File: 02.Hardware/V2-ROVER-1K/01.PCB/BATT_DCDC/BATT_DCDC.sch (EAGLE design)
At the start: 49 parts, among them J1 DF40C-20DP-0.4V_51_, K1 FLEX8, Q1 NVTFS9D6P04M8LTAG, Q2 2N7002PW, Q5 2N7002PW, U1 MCP6071T-E/OT, U3 TPS55330RTET, U7 MCP6071T-E/OT

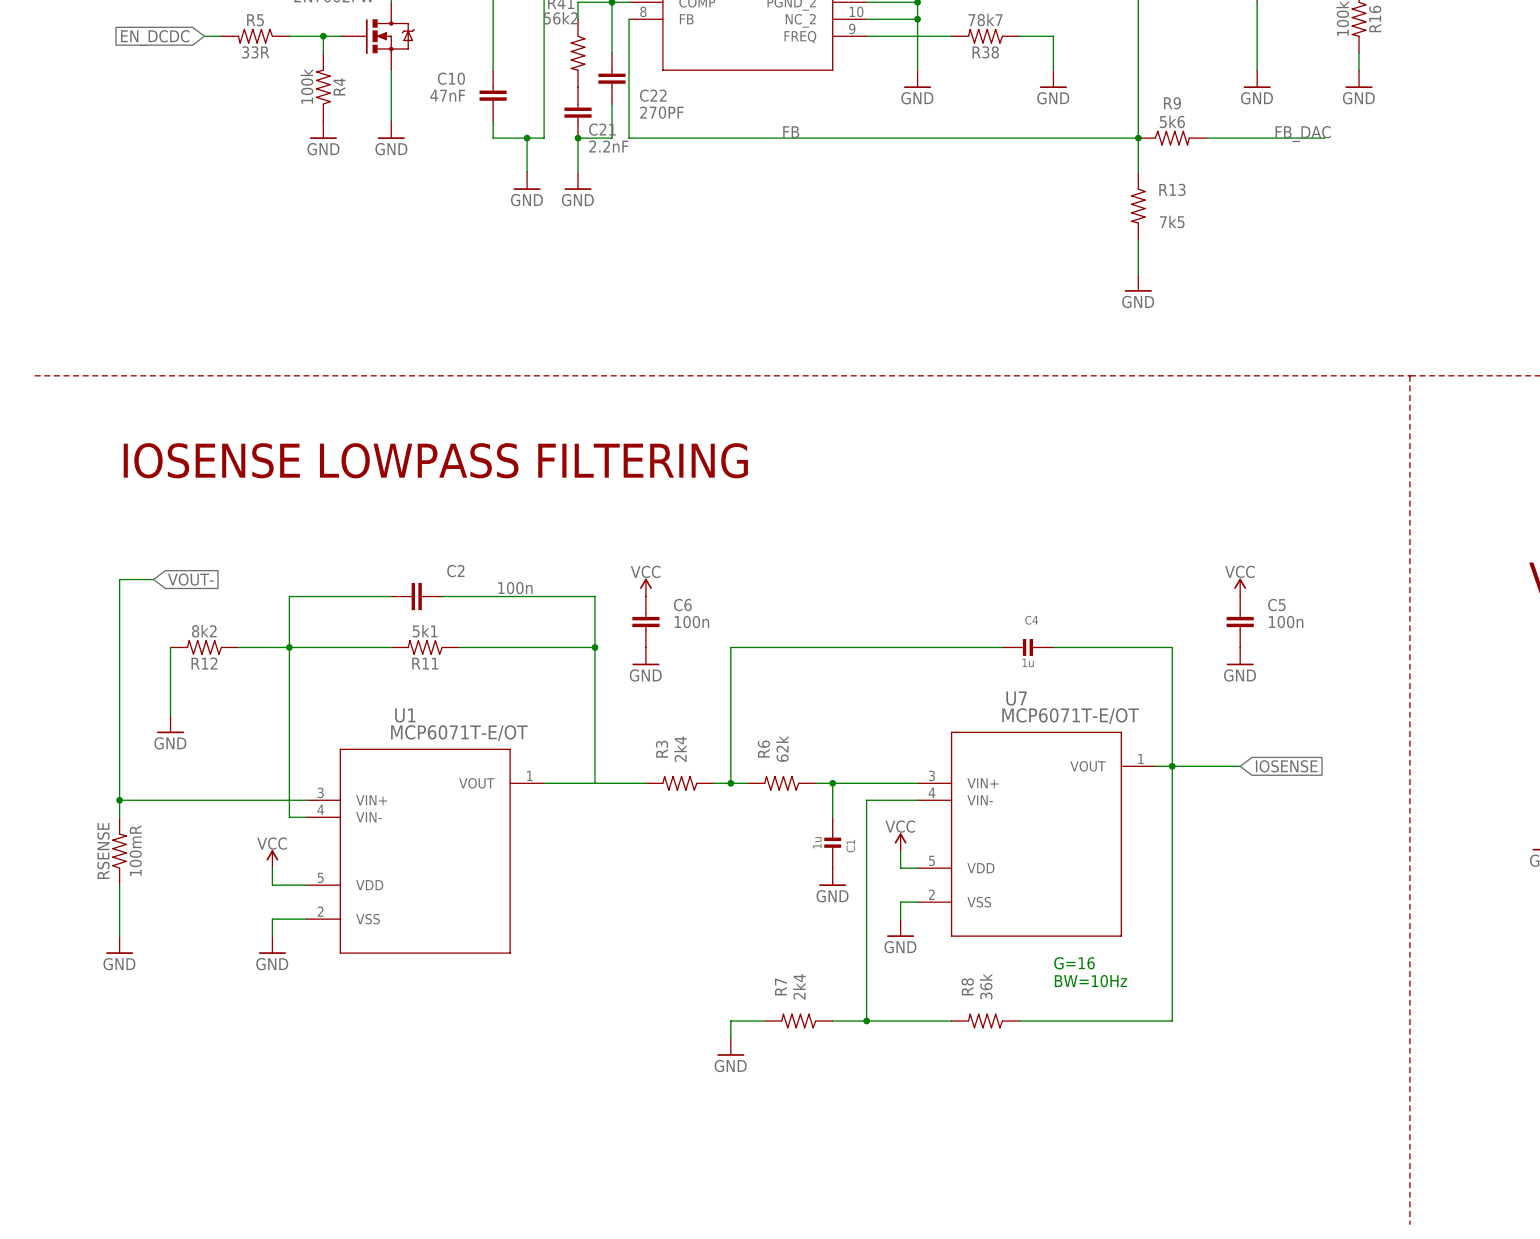
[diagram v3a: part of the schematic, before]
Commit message: Cambios menores durante revision de proto_1 de SETI
en el esquematico se incluye la frecuencia del FPB del sensado de corriente
en la BRD se aumenta el ancho de la pista de resistencia del DAC
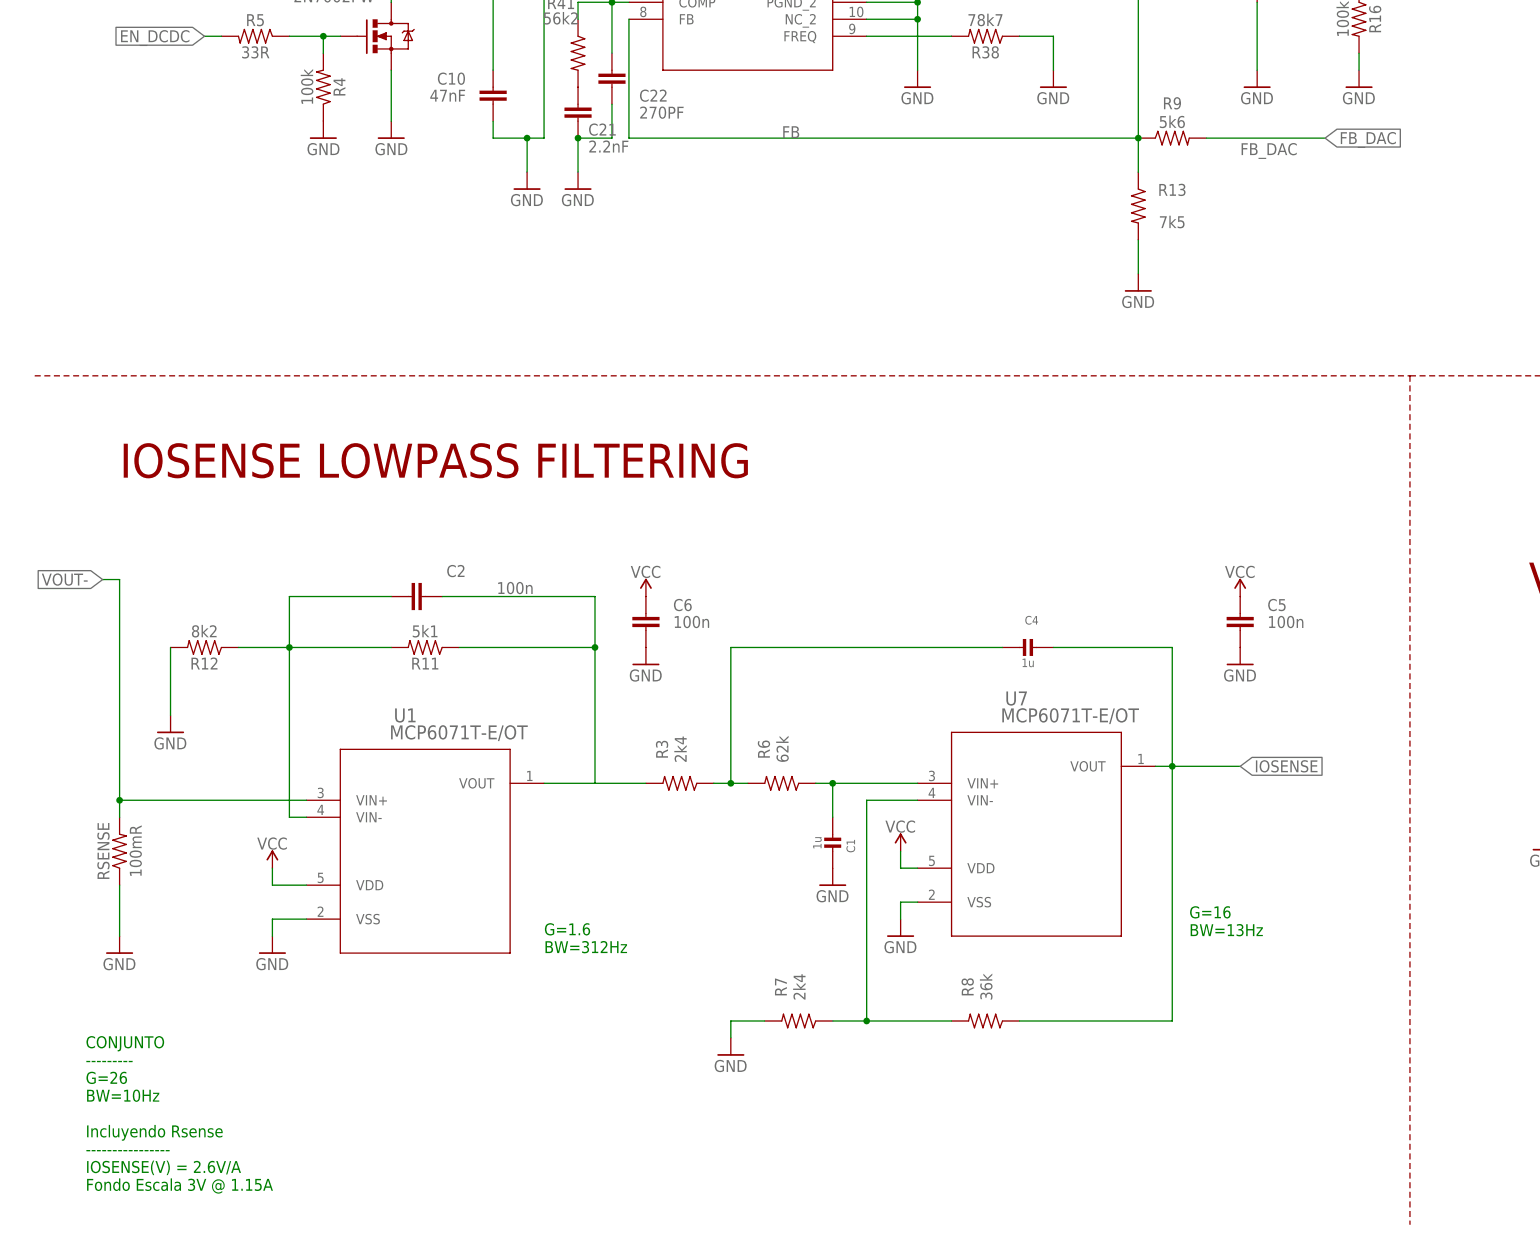
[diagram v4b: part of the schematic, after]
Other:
- note added: "CONJUNTO --------- G=26 BW=10Hz Incluyendo Rsense ---------------- IOSENSE(V) = 2.6V/A Fondo Escala 3V @ 1.15A"
- note added: "G=1.6 BW=312Hz"
- note added: "G=16 BW=13Hz"
- note removed: "G=16 BW=10Hz"
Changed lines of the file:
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@@
 <drawing>
 <settings>
-<setting alwaysvectorfont="yes"/>
+<setting alwaysvectorfont="no"/>
 <setting keepoldvectorfont="yes"/>
 <setting verticaltext="up"/>
@@
 3.0 v @ vi=16v</text>
 <text x="228.6" y="99.06" size="5.08" layer="94">VOUT SENSE</text>
-<text x="157.48" y="40.64" size="1.778" layer="91">G=16
-BW=10Hz</text>
+<text x="177.8" y="48.26" size="1.778" layer="91">G=16
+BW=13Hz</text>
 <wire x1="5.08" y1="132.08" x2="210.82" y2="132.08" width="0.1524" layer="94" style="shortdash"/>
 <wire x1="210.82" y1="132.08" x2="287.02" y2="132.08" width="0.1524" layer="94" style="shortdash"/>
@@
 <text x="35.56" y="241.3" size="5.08" layer="94">STEP UP DCDC CONVERTER
 ROVER1K - NOV'22-v1</text>
+<text x="81.28" y="45.72" size="1.778" layer="91">G=1.6
+BW=312Hz</text>
+<text x="12.7" y="10.16" size="1.778" layer="91">CONJUNTO
+---------
+G=26
+BW=10Hz
+Incluyendo Rsense
+----------------
+IOSENSE(V) = 2.6V/A
+Fondo Escala 3V @ 1.15A</text>
 </plain>
 <instances>
@@
 <pinref part="R9" gate="G$1" pin="2"/>
 <wire x1="180.34" y1="167.64" x2="198.12" y2="167.64" width="0.1524" layer="91"/>
-<label x="190.5" y="167.64" size="1.778" layer="95"/>
+<label x="185.42" y="165.1" size="1.778" layer="95"/>
+<label x="198.12" y="167.64" size="1.778" layer="95" xref="yes"/>
 </segment>
 <segment>
@@
 <wire x1="17.78" y1="66.04" x2="17.78" y2="68.58" width="0.1524" layer="91"/>
 <wire x1="17.78" y1="68.58" x2="17.78" y2="101.6" width="0.1524" layer="91"/>
-<wire x1="17.78" y1="101.6" x2="22.86" y2="101.6" width="0.1524" layer="91"/>
-<label x="22.86" y="101.6" size="1.778" layer="95" xref="yes"/>
+<wire x1="17.78" y1="101.6" x2="15.24" y2="101.6" width="0.1524" layer="91"/>
+<label x="15.24" y="101.6" size="1.778" layer="95" rot="MR0" xref="yes"/>
 <pinref part="U1" gate="A" pin="VIN+"/>
 <wire x1="45.72" y1="68.58" x2="17.78" y2="68.58" width="0.1524" layer="91"/>

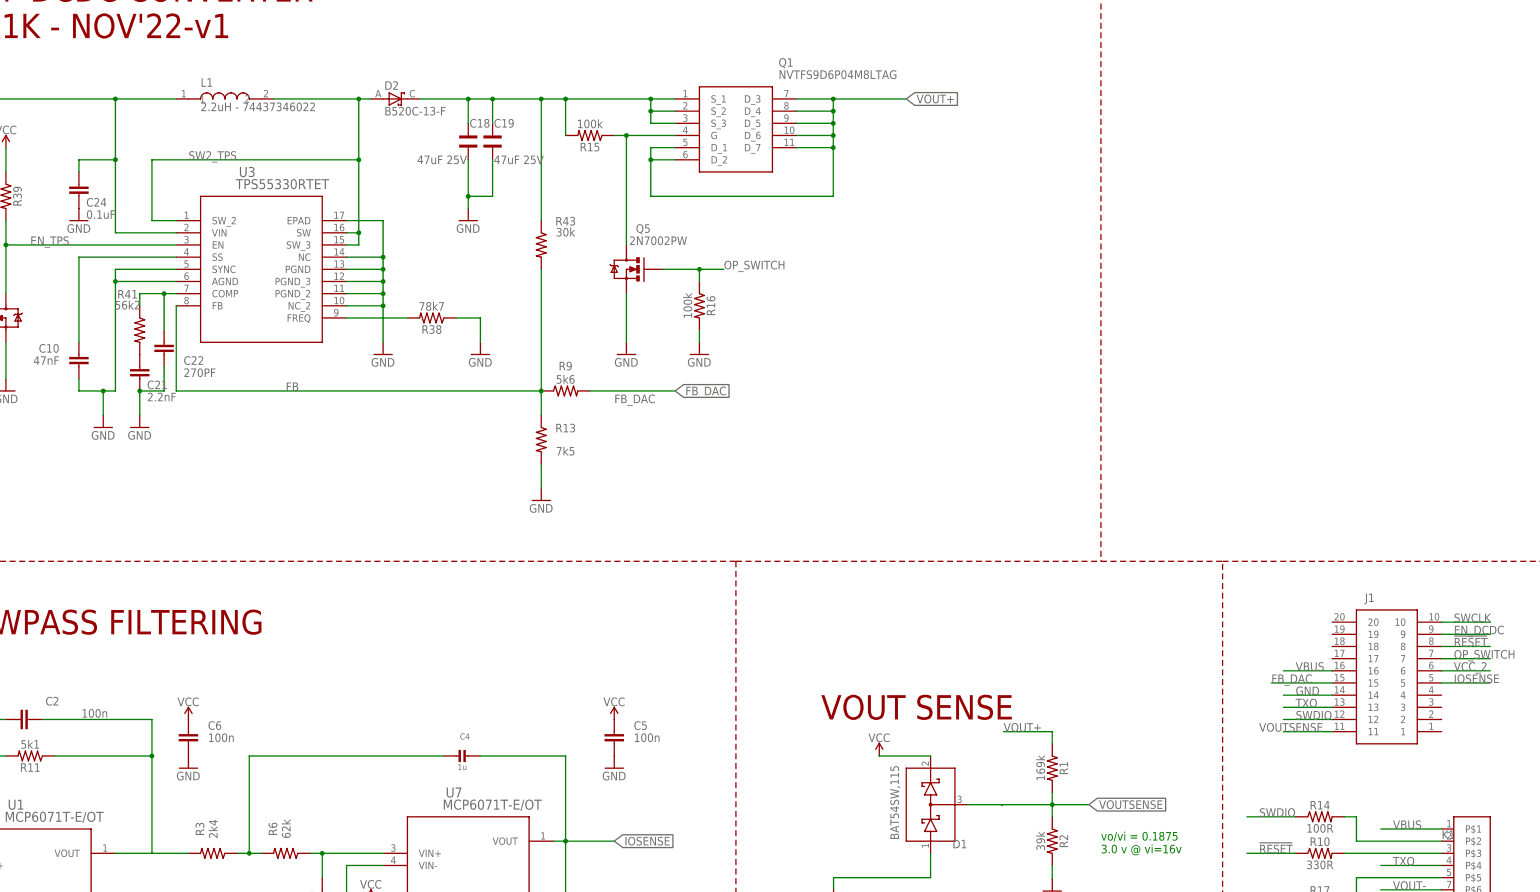
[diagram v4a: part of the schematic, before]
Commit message: Modificaciones despues de revisar 1er prototipo de SETI
Se van añadiendo modificaciones, pero no están todas las que son necesarias.
Este es el fichero que le paso a Javi para  que comience con el resto de los cambios.
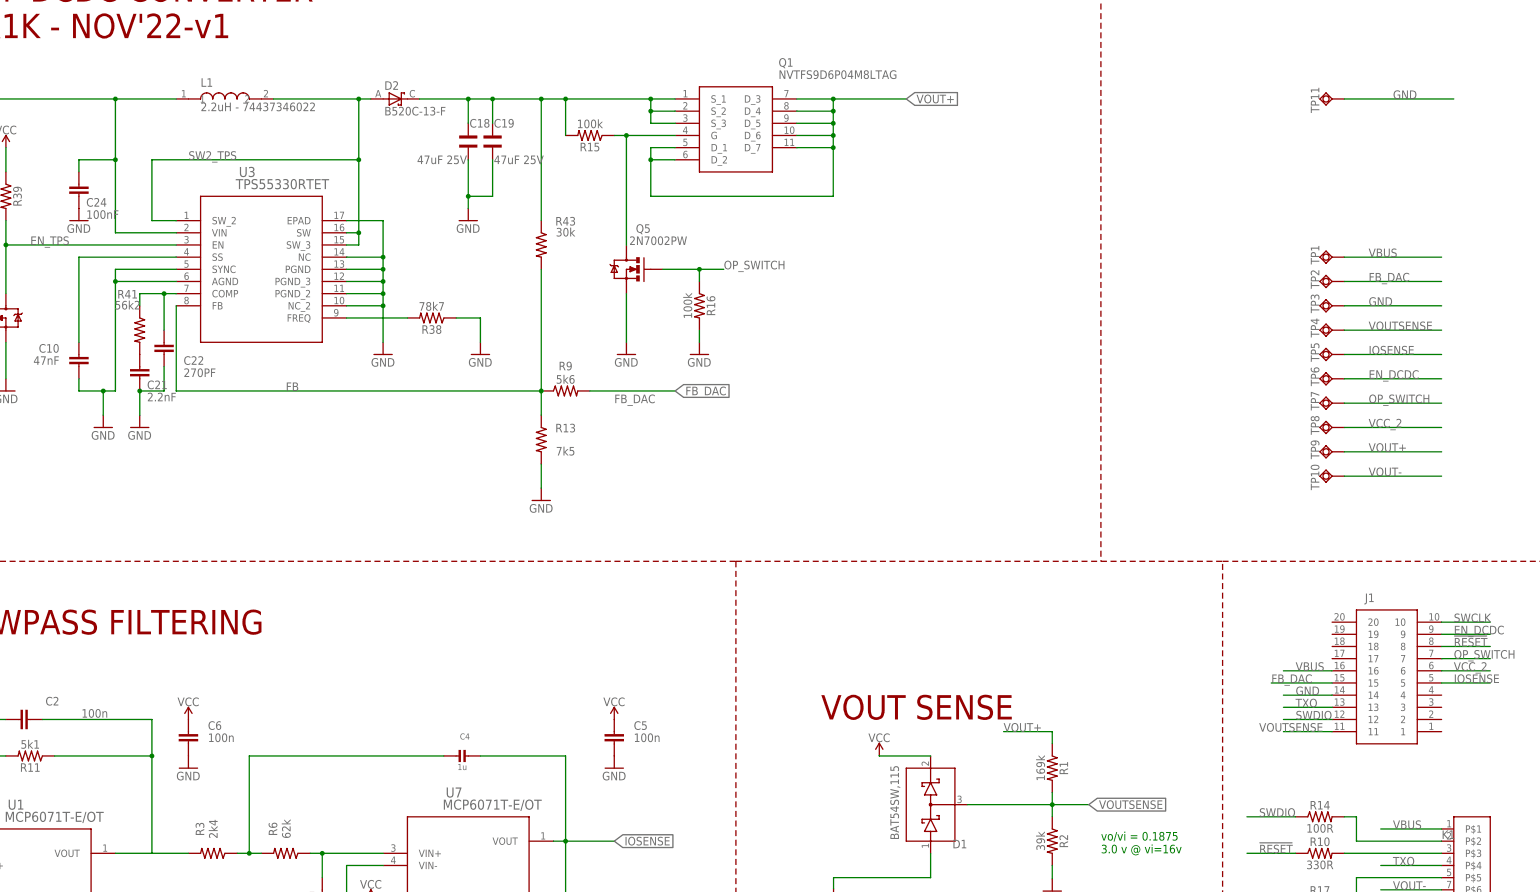
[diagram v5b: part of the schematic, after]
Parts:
- added TP1, TP10, TP11, TP2, TP3, TP4, TP5, TP6, TP7, TP8, TP9: TESTPAD_TPSQB1,27, BeagleBone_Blue_R3:TESTPAD_TPSQB1,27
- C24: value 0.1uF -> 100nF
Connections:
- net EN_DCDC: now also TP6.TP
- net FB_DAC: now also TP2.TP
- net GND: now also TP11.TP, TP3.TP
- net IOSENSE: now also TP5.TP
- net OP_SWITCH: now also TP7.TP
- net VBUS: now also TP1.TP
- net VCC_2: now also TP8.TP
- net VOUT+: now also TP9.TP
- net VOUT-: now also TP10.TP
- net VOUTSENSE: now also TP4.TP

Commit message: Cambios DCDC Javi Version Final. Pendiente de revision
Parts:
- removed TP1, TP10, TP11, TP2, TP3, TP4, TP5, TP6, TP7, TP8, TP9: TESTPAD_TPSQB1,27, BeagleBone_Blue_R3:TESTPAD_TPSQB1,27
- added C7: 220pF, SparkFun-Capacitors:270PF-0603-50V-5%
- added C8, C9: 100n, SparkFun-Capacitors:0.1UF-0603-25V-(+80/-20%)
- added EN_DCDC, FB_DAC, GND, IOSENSE, OP_SWITCH, VBUS, VCC, VOUTSENSE: TESTPAD_TPSQB1,27, BeagleBone_Blue_R3:TESTPAD_TPSQB1,27
- added R18: 0R, SparkFun-Resistors:RESISTOR0402
- C21: value 2.2nF -> 47nF
- C22: value 270PF -> 100pF
- C24: value 100nF -> 0.1uF
- K1: value FLEX8 -> FLEX11; device Flex_3mm:FLEX8 -> Flex_3mm:FLEX11
- R41: value 56k2 -> 15k
- R7: value 2k4 -> 4k3
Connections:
- removed net VCC_2: J1.6, TP8.TP
- new net N$11: K1.P$5, R14.2
- new net N$12: C9.1, R18.1, R9.2
- new net RXI: J1.15, K1.P$8
- net !RESET: now also R17.1; no longer R10.1
- net EN_DCDC: now also EN_DCDC.TP, J1.11; no longer TP6.TP
- net FB: now also C7.1
- net FB_DAC: now also FB_DAC.TP, J1.17, R18.2; no longer J1.15, R9.2, TP2.TP
- net GND: now also C8.2, C9.2, GND.TP, J1.16, J1.2, K1.P$3, K1.P$4; no longer K1.P$8, TP11.TP, TP3.TP
- net IOSENSE: now also IOSENSE.TP, J1.1; no longer J1.5, TP5.TP
- net N$10: now also K1.P$9; no longer K1.P$5
- net N$6: now also K1.P$7; no longer K1.P$3
- net N$9: now also J1.19; no longer K1.P$2, R14.2
- net OP_SWITCH: now also J1.3, J1.5, OP_SWITCH.TP; no longer J1.7, TP7.TP
- net SWCLK: now also R10.1; no longer R17.1
- net TXO: now also K1.P$6; no longer K1.P$4
- net VBUS: now also J1.18, J1.20, K1.P$2, VBUS.TP; no longer J1.16, TP1.TP
- net VCC: now also J1.4, J1.6, VCC.TP
- net VOUT+: now also K1.P$11; no longer K1.P$7, TP9.TP
- net VOUT-: now also K1.P$10; no longer K1.P$6, TP10.TP
- net VOUTSENSE: now also C8.1, J1.7, VOUTSENSE.TP; no longer J1.11, TP4.TP
- net VSOURCE: now also C7.2
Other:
- note added: "CONJUNTO --------- G=15 BW=10Hz Incluyendo Rsense ---------------- IOSENSE(V) = 1.5/A Fondo Escala 3V @ 2A"
- note added: "G=9.375 BW=13Hz"
- note removed: "CONJUNTO --------- G=26 BW=10Hz Incluyendo Rsense ---------------- IOSENSE(V) = 2.6V/A Fondo Escala 3V @ 1.15A"
- note removed: "G=16 BW=13Hz"
- moved on the sheet: R1, R10, R14, R17, R2
